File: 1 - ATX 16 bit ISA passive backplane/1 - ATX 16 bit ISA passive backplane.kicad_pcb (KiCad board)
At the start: 2 copper layers, 161.3 x 181.6 mm, 106 parts, among them J1 BUS 1, J10 AB15, J11 AB15, J12 AB15, J13 AB15, J14 B15, J15 A15, J16 A15, J17 3.3V BYPASS, J18 ATX POWER, J19 -5V BYPASS, J2 BUS 2, J20 PWR SW, J21 RST POL, J22 ACT LED, J23 RST SW, J24 RST LED, J25 PWR LED, J3 BUS 3, J4 BUS 4, J5 BUS 5, J6 BUS 6, J7 BUS 7, J8 BREADBOARD HEADER (RC2014 COM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, J9 EXTENDED HEADER, SW1 POWER, SW2 RESET, U1 74HCT14, U2 LM7905, U3 74HCT74

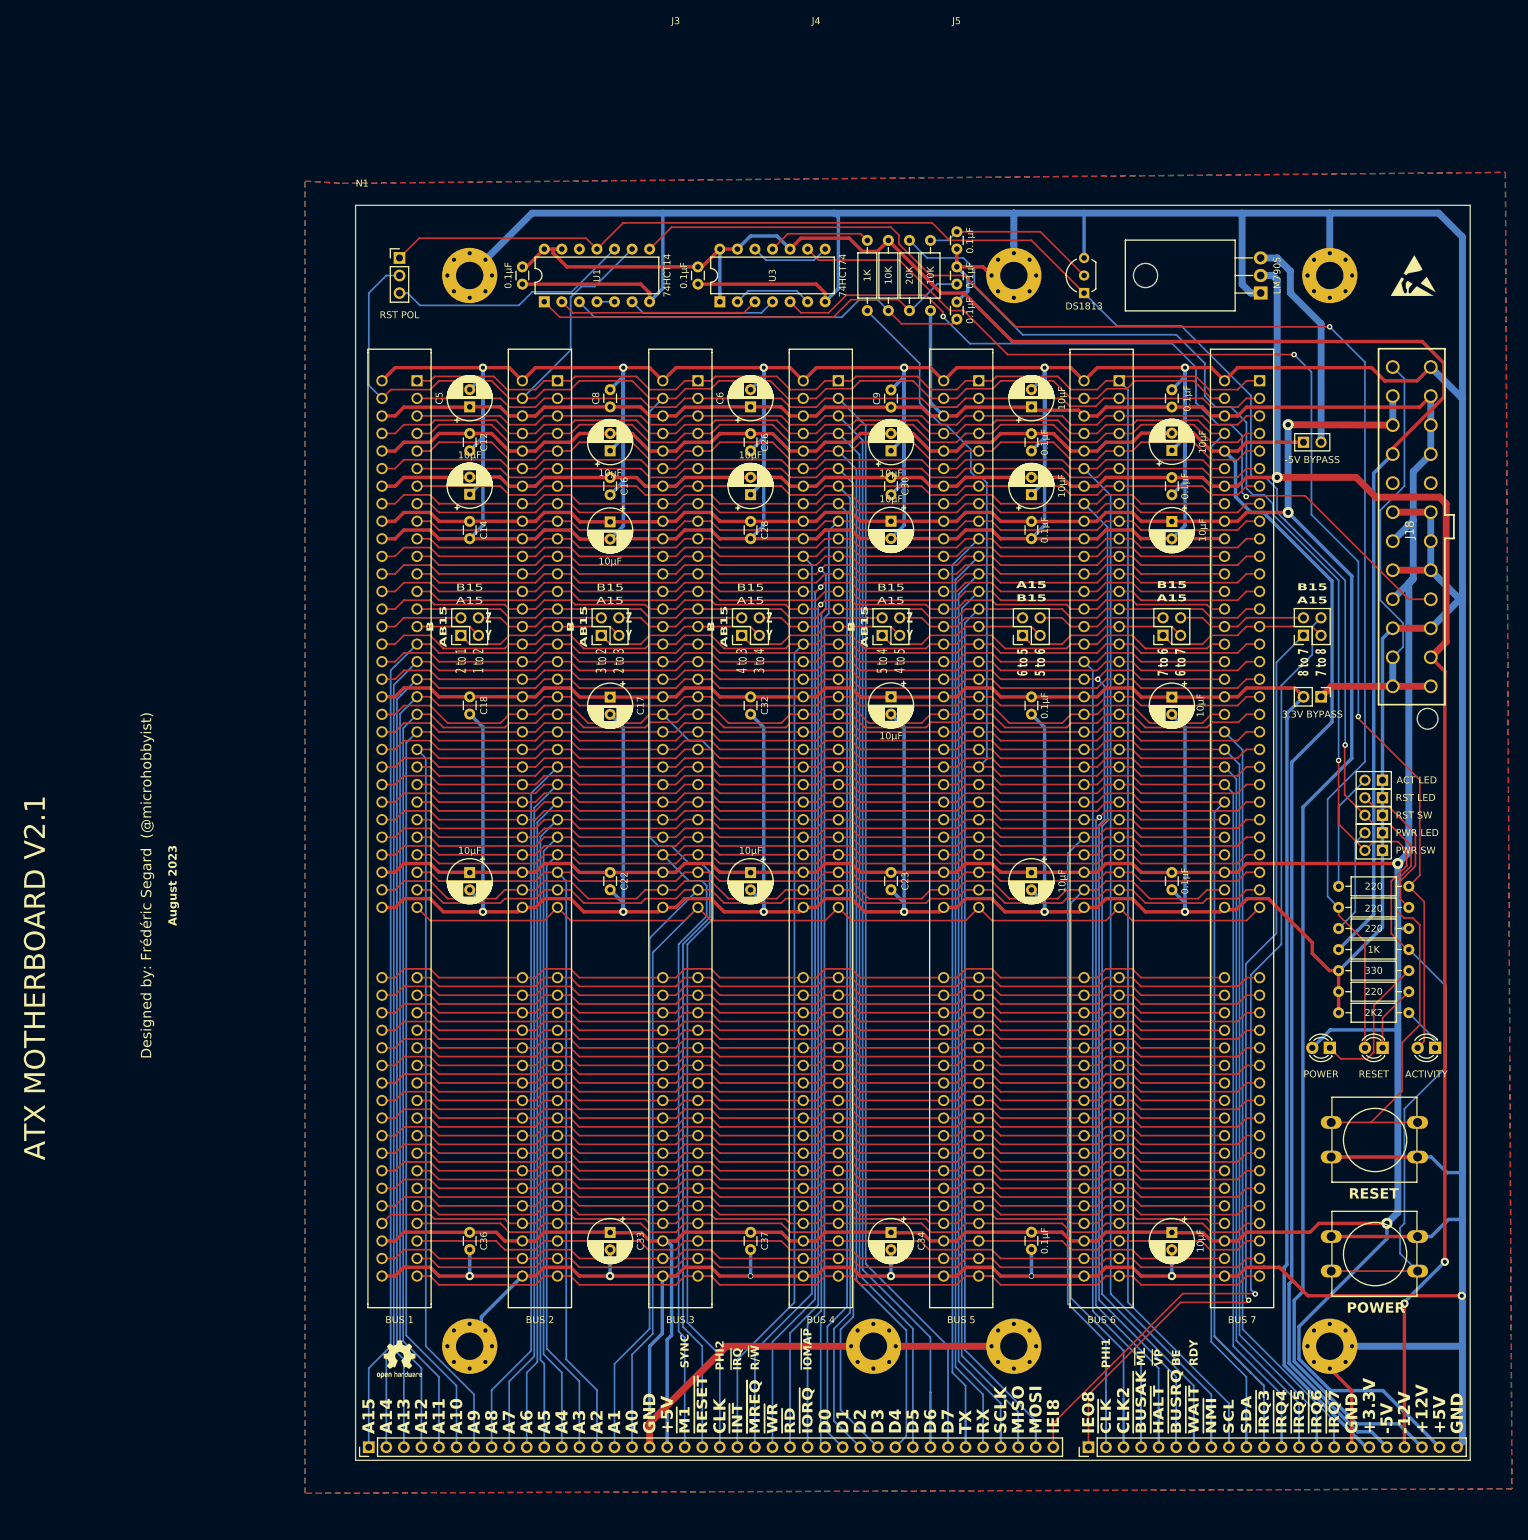
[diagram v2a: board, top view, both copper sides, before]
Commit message: Finished the silkscreen and outputed the Gerber
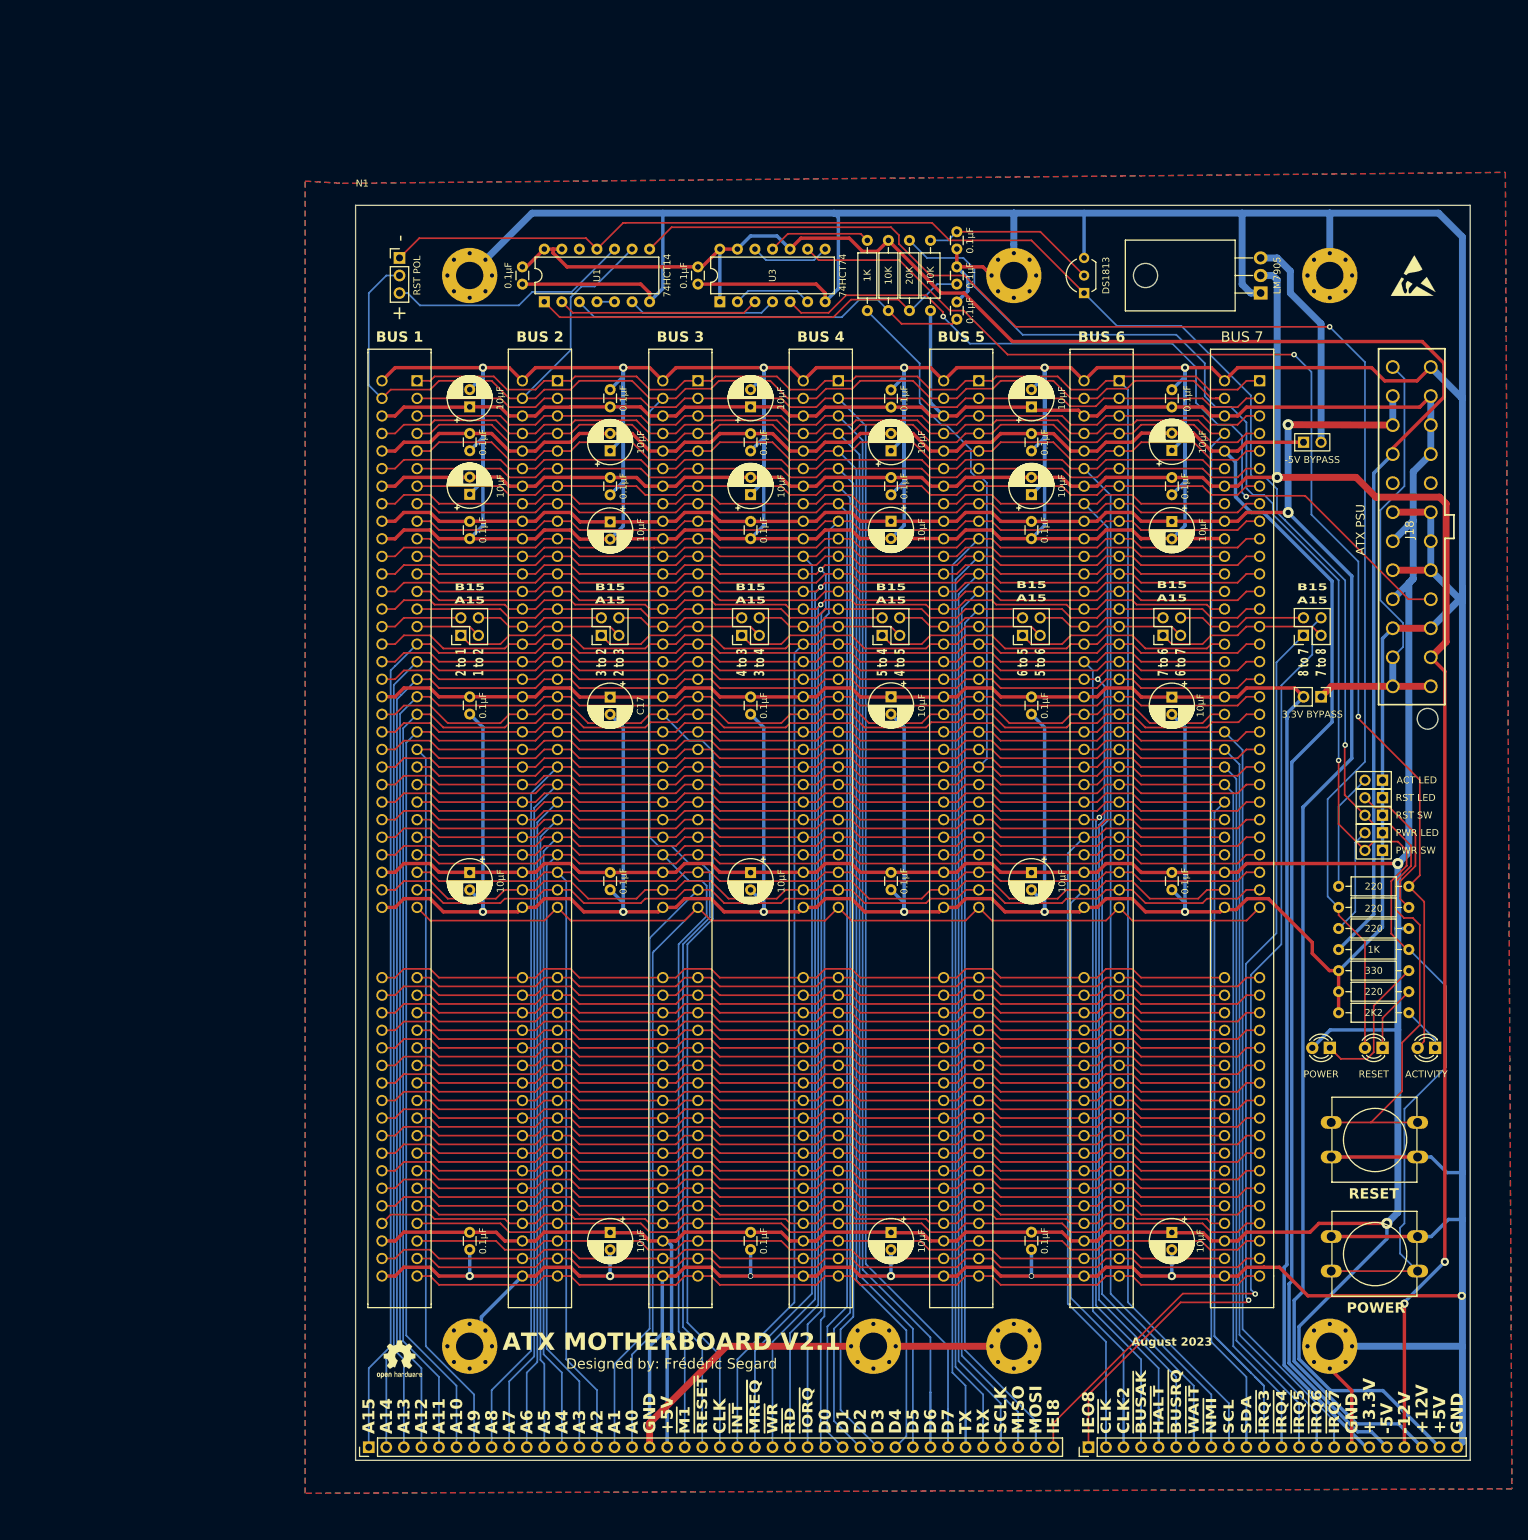
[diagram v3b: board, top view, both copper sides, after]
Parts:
- J10, J11, J12, J13: value AB15 -> A15
- J14: value B15 -> A15
- J18: value ATX POWER -> ATX PSU
- moved LOGO3 81.3 mm to (138.4, 181.5)
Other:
- board text added: "Designed by: Frédéric Segard"
- board text added: "Made in Canada www.youtube.com/@microhobbyist www.github.com/FredericSegard"
- board text removed: "1 to 2"
- board text removed: "2 to 1"
- board text removed: "2 to 3"
- board text removed: "3 to 2"
- board text removed: "3 to 4"
- board text removed: "4 to 3"
- board text removed: "4 to 5"
- board text removed: "5 to 4"
- board text removed: "B15"
- board text removed: "BE"
- board text removed: "PHI1"
- board text removed: "PHI2"
- board text removed: "R/~{W}"
- board text removed: "RDY"
- board text removed: "SYNC"
- board text removed: "www.youtube.com/@microhobbyist www.github.com/FredericSegard"
- board text removed: "~{IOMAP}"
- board text removed: "~{IRQ}"
- board text removed: "~{ML}"
- board text removed: "~{VP}"

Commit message: Minor tweaks to the backplane, and will be sending it out for manufacture
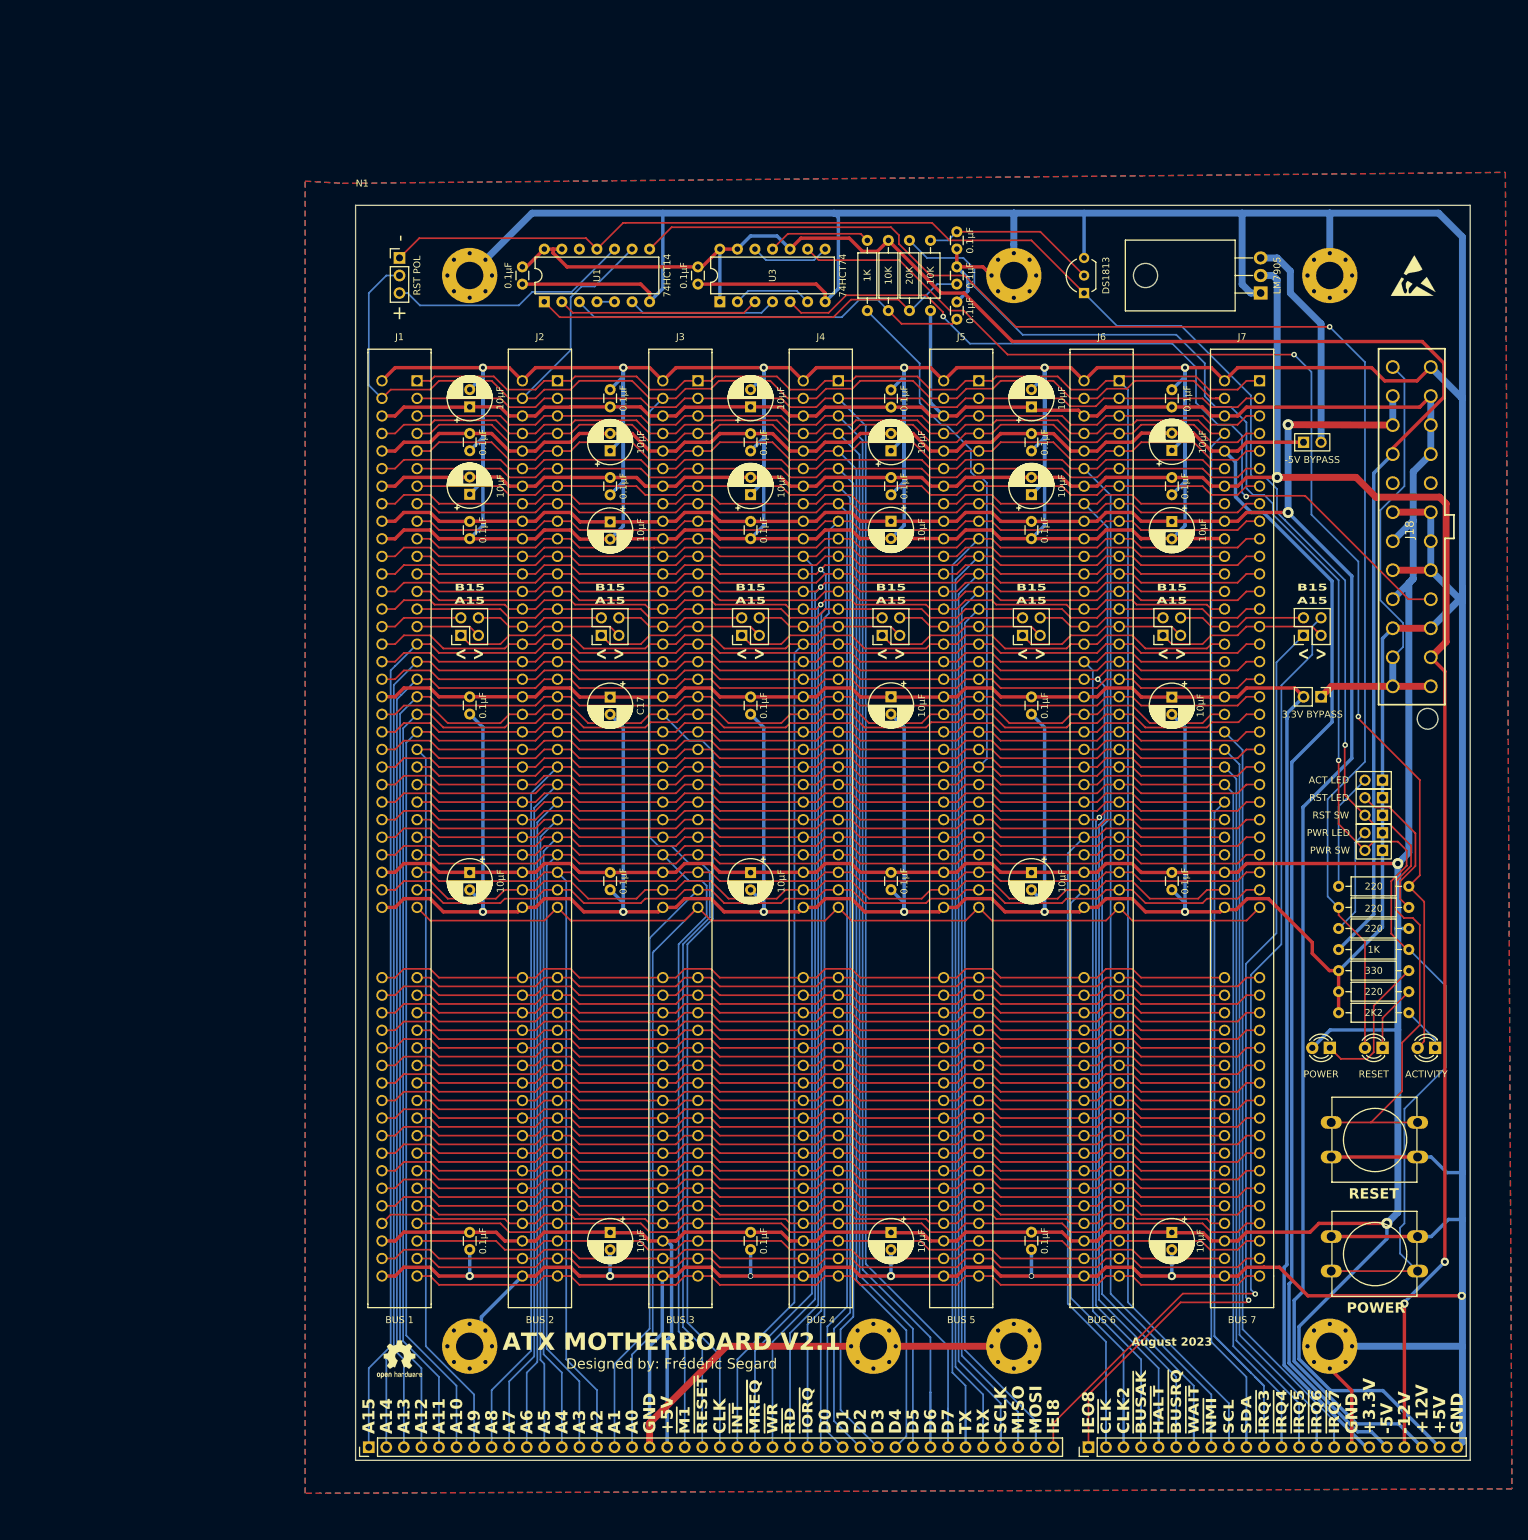
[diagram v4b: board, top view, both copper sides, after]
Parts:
- H1, H2, H3, H4, H5, H6, H7: footprint 0 - Library:MountingHole_M3.96_Pad_Via_ATX -> 0_Library:MountingHole_M3.96_Pad_Via_ATX
- J1, J2, J3, J4, J5, J6, J7: footprint 0 - Library:ISA_Connector_98 -> 0_Library:ISA_Connector_98
- J10, J11, J12, J13, J14, J15, J16: value A15 -> AB15; footprint 0 - Library:PinHeader_2x2_Vertical (Modified) -> 0_Library:PinHeader_2x2_Vertical (Modified)
- J18: value ATX PSU -> ATX POWER; footprint 0 - Library:ATX_PSU_CONN -> 0_Library:ATX_PSU_CONN
- J19, J20, J22, J23, J24, J25: footprint 0 - Library:PinHeader_1x2_Vertical (Modified) -> 0_Library:PinHeader_1x2_Vertical (Modified)
- LOGO1: footprint 0 - Library:MicroHobbyist -> 0_Library:MicroHobbyist
- LOGO3: footprint 0 - Library:JLCPCB Logo 3 -> 0_Library:JLCPCB Logo 3
- N1: footprint 0 - Library:ATX_Backplane -> 0_Library:ATX_Backplane
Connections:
- J1 pad 63: /TX2 -> /~{BANK}
- J1 pad 72: /RX2 -> /CTCLK
- J1 pad 81: /USR1 -> /~{IRQ8}
- J1 pad 82: /USR2 -> /~{IRQ9}
- J1 pad 87: /~{IRQ15} -> /~{IRQ14}
- J1 pad 88: /~{IRQ14} -> /~{IRQ15}
- J1 pad 89: /USR3 -> /USR1
- J1 pad 90: /USR4 -> /USR2
- J1 pad 91: /USR5 -> /USR3
- J1 pad 92: /USR6 -> /USR4
- J1 pad 93: /USR7 -> /USR5
- J1 pad 94: /USR8 -> /USR6
- J1 pad 95: /USR9 -> /TX2
- J1 pad 97: /USR10 -> /RX2
- J2 pad 63: /TX2 -> /~{BANK}
- J2 pad 72: /RX2 -> /CTCLK
- J2 pad 81: /USR1 -> /~{IRQ8}
- J2 pad 82: /USR2 -> /~{IRQ9}
- J2 pad 87: /~{IRQ15} -> /~{IRQ14}
- J2 pad 88: /~{IRQ14} -> /~{IRQ15}
- J2 pad 89: /USR3 -> /USR1
- J2 pad 90: /USR4 -> /USR2
- J2 pad 91: /USR5 -> /USR3
- J2 pad 92: /USR6 -> /USR4
- J2 pad 93: /USR7 -> /USR5
- J2 pad 94: /USR8 -> /USR6
- J2 pad 95: /USR9 -> /TX2
- J2 pad 97: /USR10 -> /RX2
- J3 pad 63: /TX2 -> /~{BANK}
- J3 pad 72: /RX2 -> /CTCLK
- J3 pad 81: /USR1 -> /~{IRQ8}
- J3 pad 82: /USR2 -> /~{IRQ9}
- J3 pad 87: /~{IRQ15} -> /~{IRQ14}
- J3 pad 88: /~{IRQ14} -> /~{IRQ15}
- J3 pad 89: /USR3 -> /USR1
- J3 pad 90: /USR4 -> /USR2
- J3 pad 91: /USR5 -> /USR3
- J3 pad 92: /USR6 -> /USR4
- J3 pad 93: /USR7 -> /USR5
- J3 pad 94: /USR8 -> /USR6
- J3 pad 95: /USR9 -> /TX2
- J3 pad 97: /USR10 -> /RX2
- J4 pad 63: /TX2 -> /~{BANK}
- J4 pad 72: /RX2 -> /CTCLK
- J4 pad 81: /USR1 -> /~{IRQ8}
- J4 pad 82: /USR2 -> /~{IRQ9}
- J4 pad 87: /~{IRQ15} -> /~{IRQ14}
- J4 pad 88: /~{IRQ14} -> /~{IRQ15}
- J4 pad 89: /USR3 -> /USR1
- J4 pad 90: /USR4 -> /USR2
- J4 pad 91: /USR5 -> /USR3
- J4 pad 92: /USR6 -> /USR4
- J4 pad 93: /USR7 -> /USR5
- J4 pad 94: /USR8 -> /USR6
- J4 pad 95: /USR9 -> /TX2
- J4 pad 97: /USR10 -> /RX2
- J5 pad 63: /TX2 -> /~{BANK}
- J5 pad 72: /RX2 -> /CTCLK
- J5 pad 81: /USR1 -> /~{IRQ8}
- J5 pad 82: /USR2 -> /~{IRQ9}
- J5 pad 87: /~{IRQ15} -> /~{IRQ14}
- J5 pad 88: /~{IRQ14} -> /~{IRQ15}
- J5 pad 89: /USR3 -> /USR1
- J5 pad 90: /USR4 -> /USR2
- J5 pad 91: /USR5 -> /USR3
- J5 pad 92: /USR6 -> /USR4
- J5 pad 93: /USR7 -> /USR5
- J5 pad 94: /USR8 -> /USR6
- J5 pad 95: /USR9 -> /TX2
- J5 pad 97: /USR10 -> /RX2
- J6 pad 63: /TX2 -> /~{BANK}
- J6 pad 72: /RX2 -> /CTCLK
- J6 pad 81: /USR1 -> /~{IRQ8}
- J6 pad 82: /USR2 -> /~{IRQ9}
- J6 pad 87: /~{IRQ15} -> /~{IRQ14}
- J6 pad 88: /~{IRQ14} -> /~{IRQ15}
- J6 pad 89: /USR3 -> /USR1
- J6 pad 90: /USR4 -> /USR2
- J6 pad 91: /USR5 -> /USR3
- J6 pad 92: /USR6 -> /USR4
- J6 pad 93: /USR7 -> /USR5
- J6 pad 94: /USR8 -> /USR6
- J6 pad 95: /USR9 -> /TX2
- J6 pad 97: /USR10 -> /RX2
- J7 pad 63: /TX2 -> /~{BANK}
- J7 pad 72: /RX2 -> /CTCLK
- J7 pad 81: /USR1 -> /~{IRQ8}
- J7 pad 82: /USR2 -> /~{IRQ9}
- J7 pad 87: /~{IRQ15} -> /~{IRQ14}
- J7 pad 88: /~{IRQ14} -> /~{IRQ15}
- J7 pad 89: /USR3 -> /USR1
- J7 pad 90: /USR4 -> /USR2
- J7 pad 91: /USR5 -> /USR3
- J7 pad 92: /USR6 -> /USR4
- J7 pad 93: /USR7 -> /USR5
- J7 pad 94: /USR8 -> /USR6
- J7 pad 95: /USR9 -> /TX2
- J7 pad 97: /USR10 -> /RX2
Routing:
- net /USR9: track 128.2 -> 0.00 mm
- net /~{BANK}: track 0.00 -> 128.2 mm
- net /USR8: track 128.2 -> 0.00 mm
- net /~{IRQ8}: track 0.00 -> 128.2 mm
- net /~{IRQ9}: track 0.00 -> 128.2 mm
- net /USR7: track 128.2 -> 0.00 mm
- net /USR10: track 128.2 -> 0.00 mm
- net /CTCLK: track 0.00 -> 128.2 mm
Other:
- board text added: "<"
- board text added: ">"
- board text added: "B15"
- board text removed: "Designed by: Frédéric Segard (@microhobbyist)"
